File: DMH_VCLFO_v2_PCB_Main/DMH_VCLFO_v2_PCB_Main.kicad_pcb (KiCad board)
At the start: 2 copper layers, 98 x 175 mm, 77 parts, among them J1 TS_Jack_6.35mm_Sw, J10 TS_Jack_6.35mm_Sw, J100 IDC_02x08, J11 TS_Jack_6.35mm_Sw, J12 TS_Jack_6.35mm_Sw, J13 TS_Jack_6.35mm_Sw, J14 TS_Jack_6.35mm_Sw, J15 TS_Jack_6.35mm_Sw, J16 TS_Jack_6.35mm_Sw, J17 TS_Jack_6.35mm_Sw, J18 TS_Jack_6.35mm_Sw, J2 TS_Jack_6.35mm_Sw, J21 IDC_02x05, J22 Conn_01x08, J23 Conn_01x08, J27 Conn_01x08, J28 Conn_01x08, J3 TS_Jack_6.35mm_Sw, J32 Conn_01x08, J33 Conn_01x08, J35 Conn_02x03_Odd_Even, J37 Conn_02x03_Odd_Even, J39 Conn_02x03_Odd_Even, J4 TS_Jack_6.35mm_Sw, J41 Conn_02x03_Odd_Even, J43 Conn_02x03_Odd_Even, J45 Conn_02x03_Odd_Even, J47 Conn_02x03_Odd_Even, J49 Conn_02x03_Odd_Even, J5 TS_Jack_6.35mm_Sw, J51 Conn_02x03_Odd_Even, J52 Conn_01x06, J53 Conn_01x01, J6 TS_Jack_6.35mm_Sw, J7 TS_Jack_6.35mm_Sw, J8 TS_Jack_6.35mm_Sw, J9 TS_Jack_6.35mm_Sw, U1 TL074, U2 TL074, U3 TL074

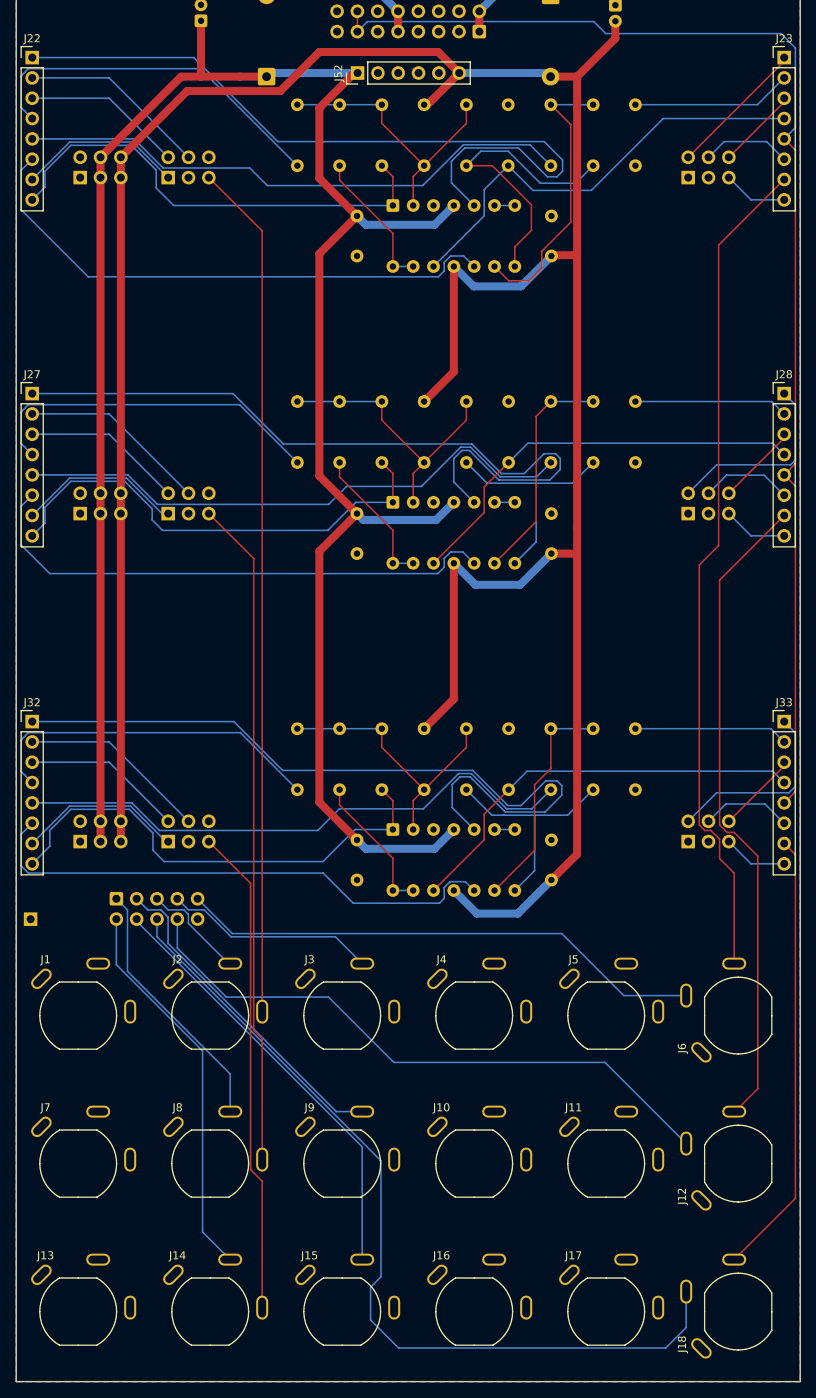
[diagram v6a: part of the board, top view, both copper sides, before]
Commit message: Main PCB routing done
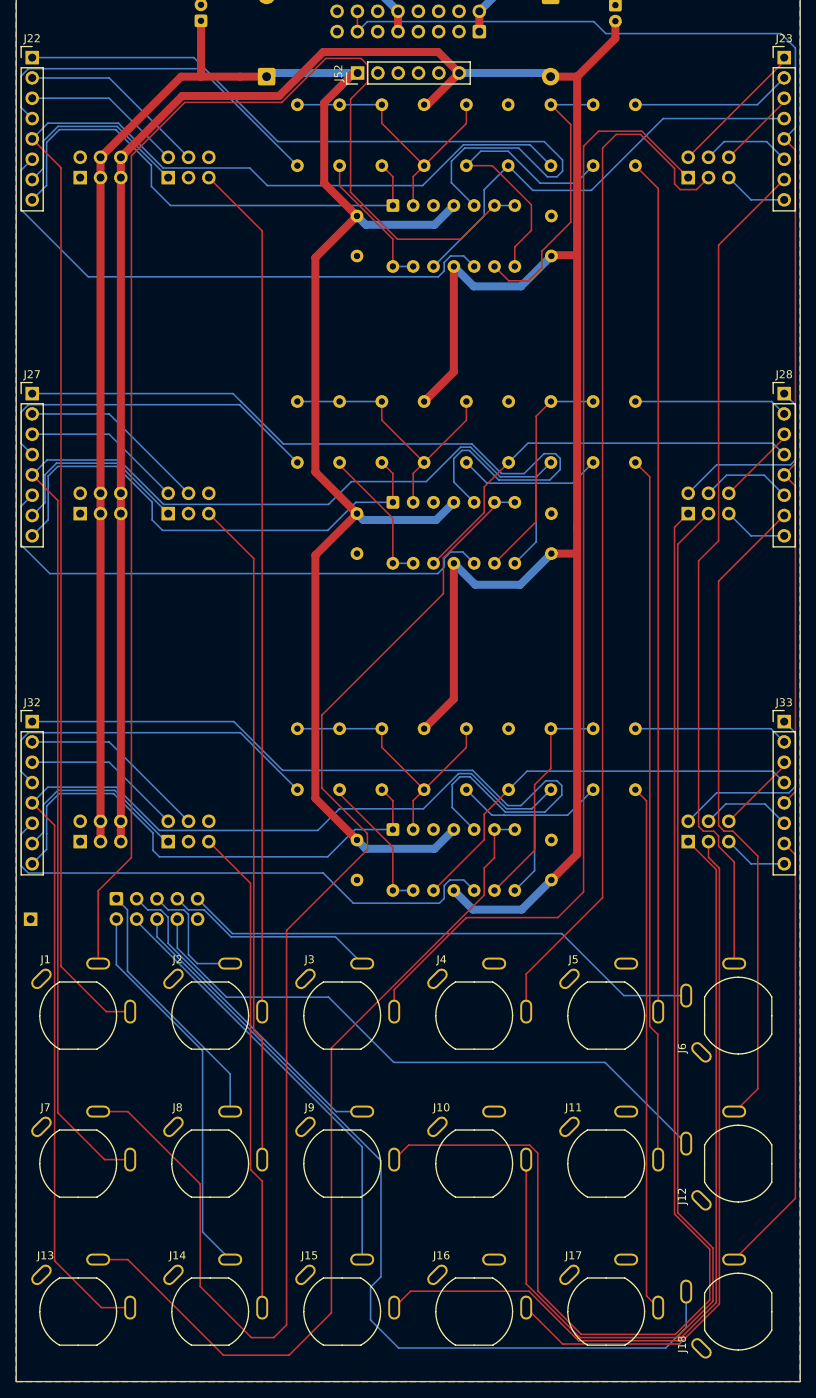
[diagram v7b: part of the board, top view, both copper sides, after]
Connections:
- J21 pad 10: GND -> unconnected-(J21-Pin_10-Pad10)
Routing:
- net Net-(U1B--): track 2.54 -> 179.1 mm
- net B_Sqr_M: track 0.00 -> 162.7 mm
- net Net-(U2B--): track 2.54 -> 164.2 mm
- net B_Saw_M: track 0.00 -> 145.4 mm
- net A_Sqr_M: track 0.00 -> 140.9 mm
- net A_Saw_M: track 0.00 -> 130.5 mm
- net A_CV_Amt_Pot_p3_M: track 70.4 -> 188.0 mm
- net Net-(J5-PadT): track 0.00 -> 106.9 mm
- net Net-(U3B--): track 2.54 -> 107.7 mm
- net C_Sqr_M: track 0.00 -> 104.7 mm
- net B_CV_Amt_Pot_p3_M: track 71.6 -> 165.7 mm
- net Net-(J11-PadT): track 0.00 -> 88.3 mm
- net C_Saw_M: track 0.00 -> 86.5 mm
- net C_CV_Amt_Pot_p3_M: track 72.0 -> 143.9 mm
- net Net-(J17-PadT): track 0.00 -> 65.9 mm
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
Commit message: Generated Gerbers
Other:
- board text added: "Mk1.0 - March 2026"
- board text removed: "Mk1.0 - Month Year"
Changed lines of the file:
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@@
 			(plot_on_all_layers_selection 0x00000000_00000000_00000000_00000000)
 			(disableapertmacros no)
-			(usegerberextensions no)
+			(usegerberextensions yes)
 			(usegerberattributes yes)
 			(usegerberadvancedattributes yes)
@@
 			(sketchdnponfab yes)
 			(crossoutdnponfab yes)
-			(subtractmaskfromsilk no)
+			(subtractmaskfromsilk yes)
 			(outputformat 1)
 			(mirror no)
-			(drillshape 1)
+			(drillshape 0)
 			(scaleselection 1)
-			(outputdirectory "")
+			(outputdirectory "Gerbers/")
 		)
 	)
@@
 		(layer "User.9")
 	)
-	(gr_text "Mk1.0 - Month Year"
+	(gr_text "Mk1.0 - March 2026"
 		(at 100 216.25 0)
 		(layer "B.SilkS")
